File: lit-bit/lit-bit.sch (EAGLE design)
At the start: 10 parts, among them IC1 ATMEGA32U4-MU, SW1 SPST_TACT-KMR2, U1 S-1317A33-M5T1U4, X3 microUSB, Y1 8MHz

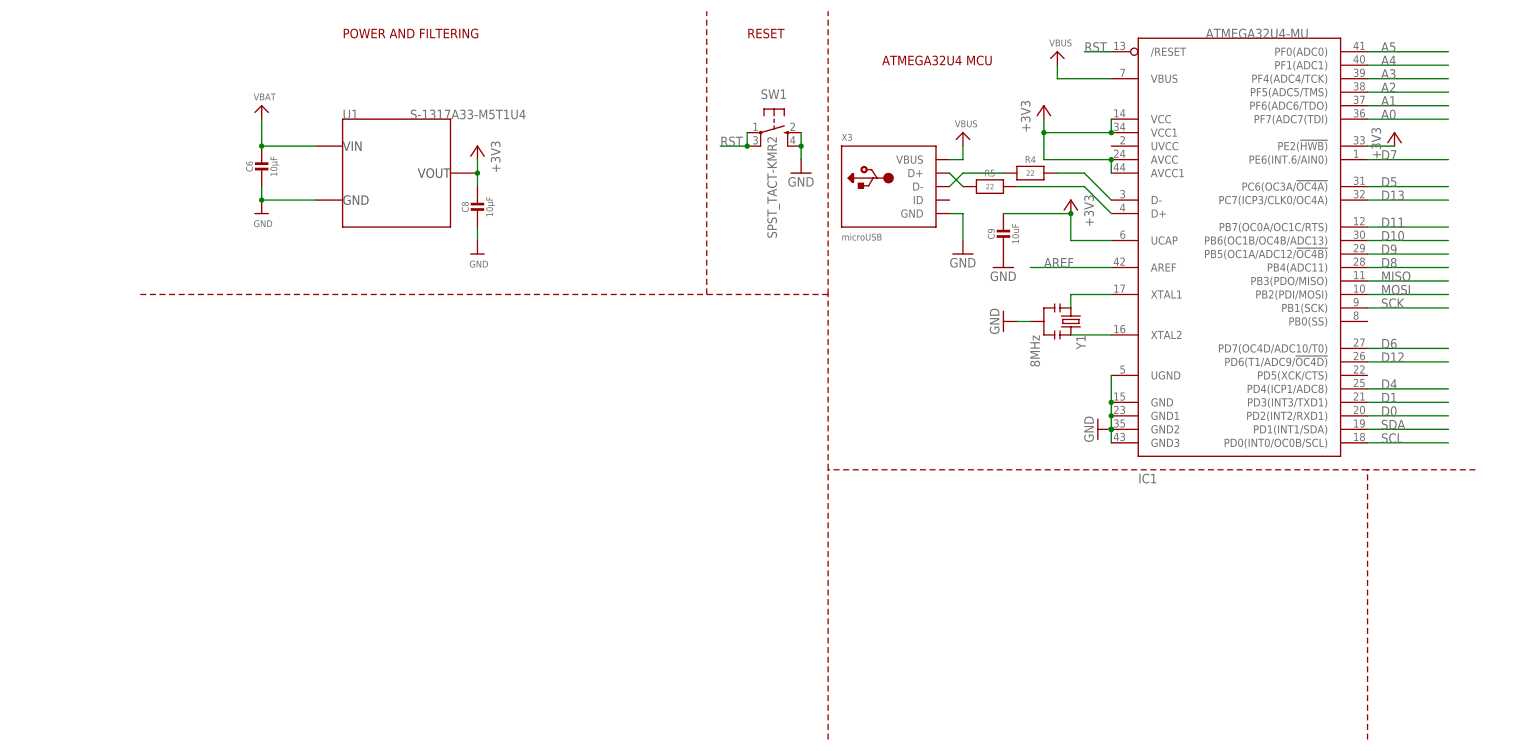
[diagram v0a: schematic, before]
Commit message: added power circuitry
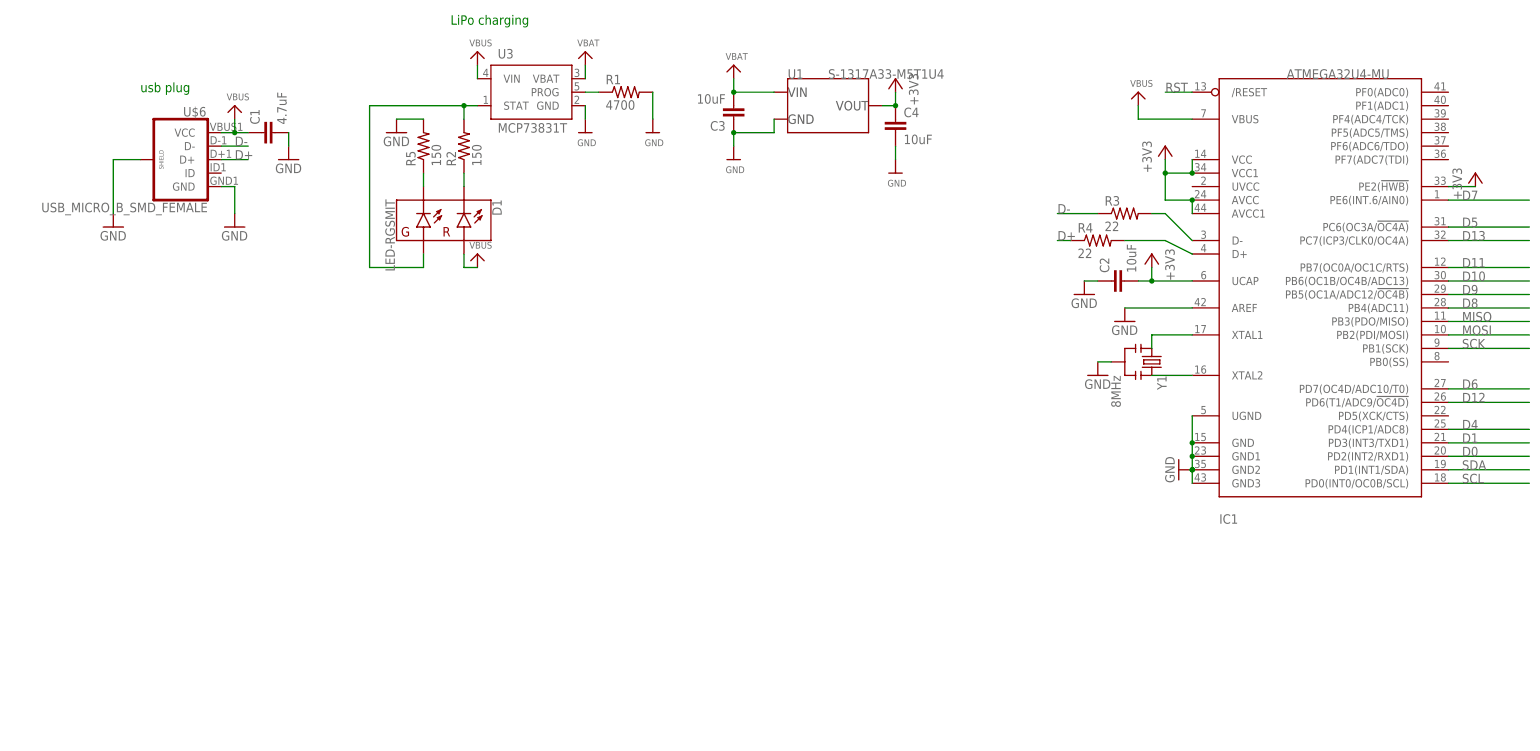
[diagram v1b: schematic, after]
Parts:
- removed C6, C8: 10µF, microbuilder:CAP_CERAMIC0805-NOOUTLINE
- removed C9: 10uF, microbuilder:CAP_CERAMIC0805-NOOUTLINE
- removed SW1: SPST_TACT-KMR2, adafruit:SPST_TACT-KMR2
- removed X3: microUSB, microbuilder:USB_MICRO_20329_V2
- added C1: 4.7uF, SCADA_CUSTOM_LIBRARY:CAP_NONPOL_0805
- added C2, C3, C4: 10uF, SCADA_CUSTOM_LIBRARY:CAP_NONPOL_0805
- added D1: LED-RGSMIT, SCADA_CUSTOM_LIBRARY:LED-RGSMIT
- added R1: 4700, SCADA_CUSTOM_LIBRARY:RES-0805
- added R2: 150, SCADA_CUSTOM_LIBRARY:RES-0805
- added R3: 22, SCADA_CUSTOM_LIBRARY:RES-0805
- added U$6: USB_MICRO_B_SMD_FEMALE, SCADA_CUSTOM_LIBRARY:USB_MICRO_B_SMD_FEMALE
- added U3: MCP73831T, SCADA_CUSTOM_LIBRARY:MCP73831T
- R4: device microbuilder:RESISTOR_0603_NOOUT -> SCADA_CUSTOM_LIBRARY:RES-0805
- R5: value 22 -> 150; device microbuilder:RESISTOR_0603_NOOUT -> SCADA_CUSTOM_LIBRARY:RES-0805
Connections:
- removed net A0: IC1.PF7(ADC7(TDI)
- removed net A1: IC1.PF6(ADC6/TDO)
- removed net A2: IC1.PF5(ADC5/TMS)
- removed net A3: IC1.PF4(ADC4/TCK)
- removed net A4: IC1.PF1(ADC1)
- removed net A5: IC1.PF0(ADC0)
- removed net AREF: IC1.AREF
- removed net N$15: R5.1, X3.D+
- removed net N$16: R4.1, X3.D-
- new net N$1: IC1.D-, R3.2
- new net N$2: R1.1, U3.PROG
- new net N$3: D1.GA, R2.2, U3.STAT
- new net N$4: D1.RC, R2.1
- new net N$5: D1.GC, R5.1
- net +3V3: now also C2.2, C4.1; no longer C8.1, C9.1
- net D+: now also R4.1, R4.2, U$6.D+; no longer R5.2
- net D-: now also R3.1, U$6.D-; no longer IC1.D-, R4.2
- net GND: now also C1.2, C2.1, C3.1, C4.2, IC1.AREF, R1.2, R5.2, U$6.GND, U$6.SHIELD, U3.GND; no longer C6.2, C8.2, C9.2, SW1.S, SW1.S1, X3.GND
- net RST: no longer SW1.P, SW1.P1
- net VBAT: now also C3.2, U3.VBAT; no longer C6.1
- net VBUS: now also C1.1, D1.RA, U$6.VCC, U3.VIN; no longer X3.VBUS
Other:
- note added: "LiPo charging"
- note added: "usb plug"
- note removed: "ATMEGA32U4 MCU"
- note removed: "POWER AND FILTERING"
- note removed: "RESET"
- moved on the sheet: IC1, U1, Y1

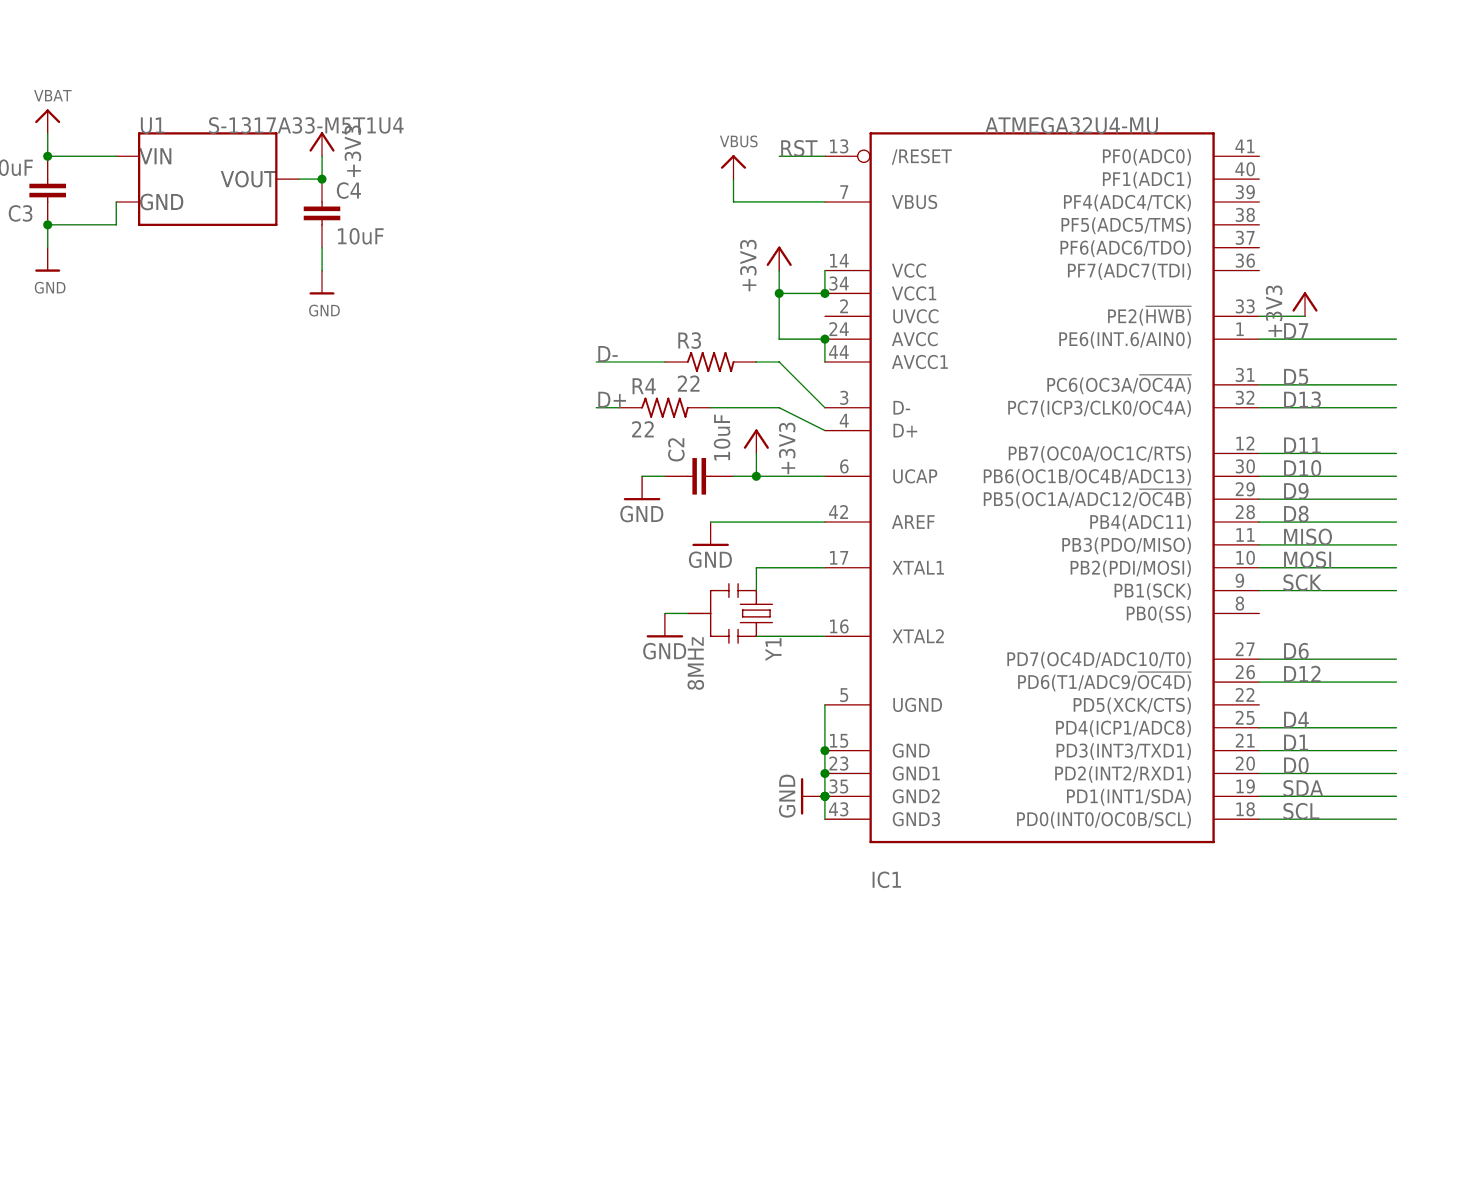
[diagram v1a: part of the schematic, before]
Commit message: imported TQFN package for 32u4
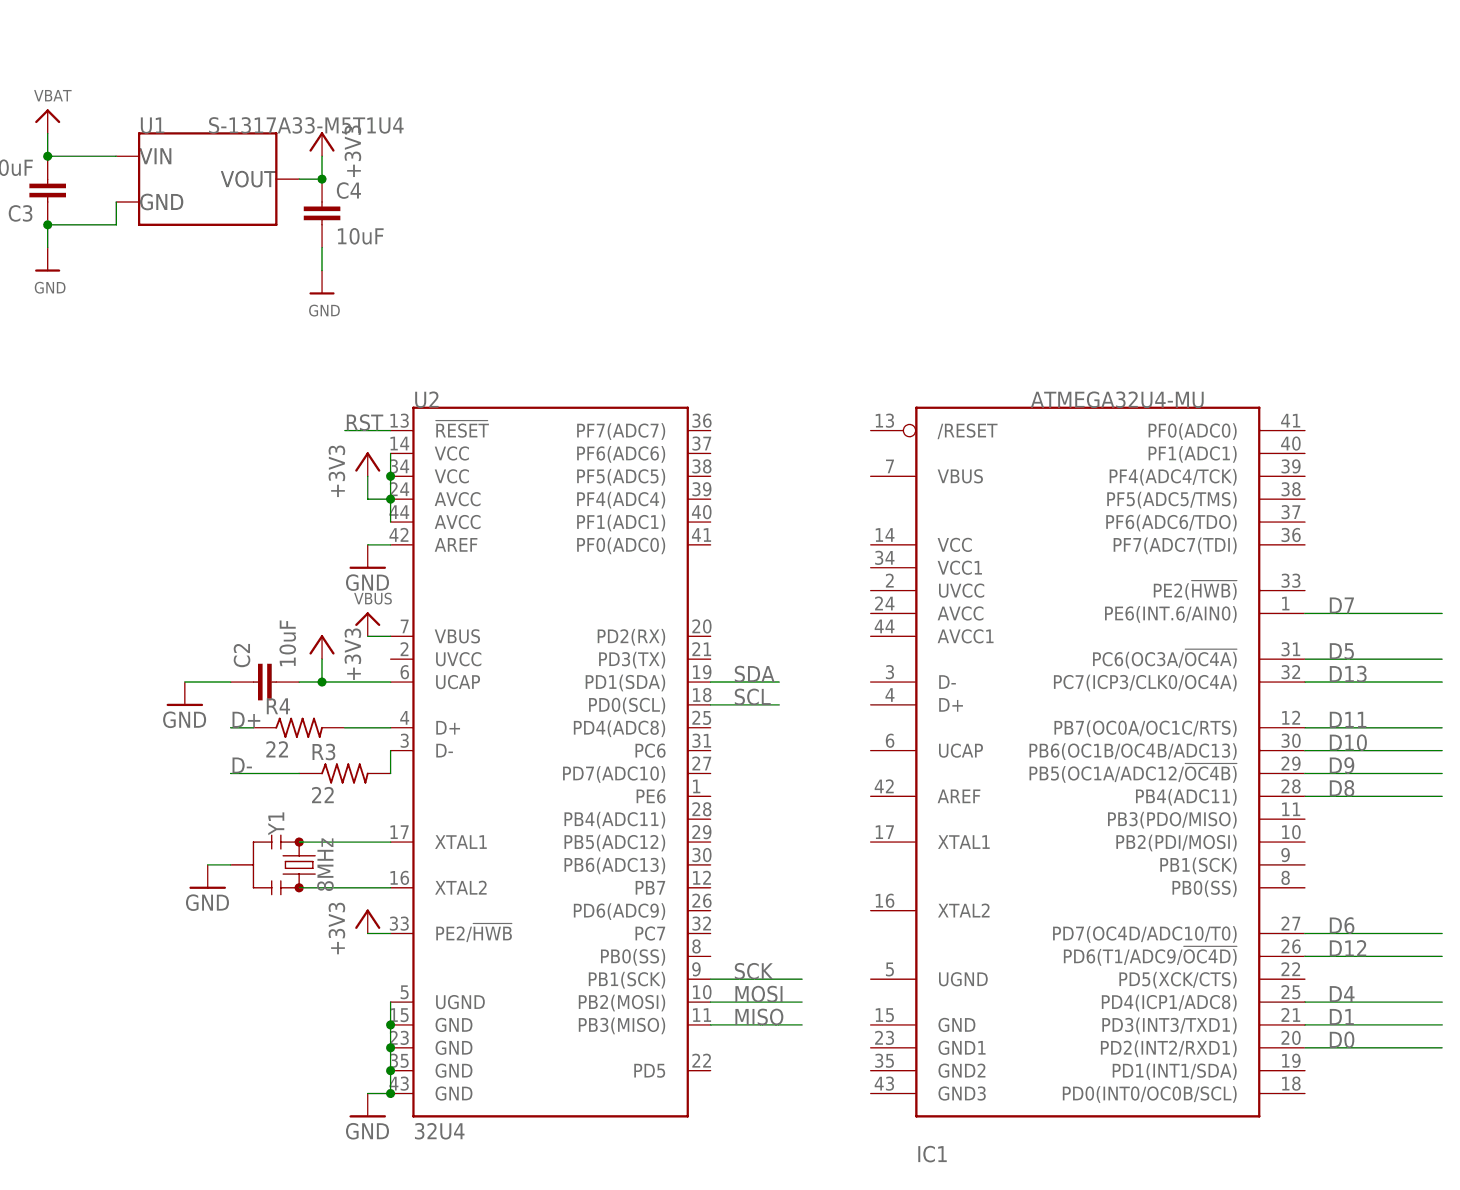
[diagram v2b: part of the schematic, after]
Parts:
- added U2: 32U4, SCADA_CUSTOM_LIBRARY:ATMEGA32U4TQFP-44
- Y1: device SparkFun:RESONATORSMD -> SCADA_CUSTOM_LIBRARY:RESONATOR-8MHZSMD_3.2X1.3
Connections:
- removed net N$11: IC1.XTAL2, Y1.3
- removed net N$12: IC1.XTAL1, Y1.1
- new net N$6: R3.2, U2.D-
- new net N$7: U2.XTAL2, Y1.3
- net +3V3: now also U2.AVCC@24, U2.AVCC@44, U2.PE2/!HWB, U2.UCAP, U2.VCC@14, U2.VCC@34; no longer IC1.AVCC, IC1.AVCC1, IC1.PE2(!HWB), IC1.UCAP, IC1.VCC, IC1.VCC1
- net D+: now also U2.D+; no longer IC1.D+
- net GND: now also U2.AREF, U2.GND@15, U2.GND@23, U2.GND@35, U2.GND@43, U2.UGND; no longer IC1.AREF, IC1.GND, IC1.GND1, IC1.GND2, IC1.GND3, IC1.UGND
- net MISO: now also U2.PB3(MISO); no longer IC1.PB3(PDO/MISO)
- net MOSI: now also U2.PB2(MOSI); no longer IC1.PB2(PDI/MOSI)
- net N$1: now also U2.XTAL1, Y1.1; no longer IC1.D-, R3.2
- net RST: now also U2.!RESET; no longer IC1./RESET
- net SCK: now also U2.PB1(SCK); no longer IC1.PB1(SCK)
- net SCL: now also U2.PD0(SCL); no longer IC1.PD0(INT0/OC0B/SCL)
- net SDA: now also U2.PD1(SDA); no longer IC1.PD1(INT1/SDA)
- net VBUS: now also U2.VBUS; no longer IC1.VBUS
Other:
- moved on the sheet: C2, IC1, R3, R4

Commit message: removed QFN 32u4
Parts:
- removed IC1: ATMEGA32U4-MU, microbuilder:ATMEGA32U4-MU
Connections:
- removed net D0: IC1.PD2(INT2/RXD1)
- removed net D1: IC1.PD3(INT3/TXD1)
- removed net D10: IC1.PB6(OC1B/OC4B/ADC13)
- removed net D11: IC1.PB7(OC0A/OC1C/RTS)
- removed net D12: IC1.PD6(T1/ADC9/!OC4D)
- removed net D13: IC1.PC7(ICP3/CLK0/OC4A)
- removed net D4: IC1.PD4(ICP1/ADC8)
- removed net D5: IC1.PC6(OC3A/!OC4A)
- removed net D6: IC1.PD7(OC4D/ADC10/T0)
- removed net D7: IC1.PE6(INT.6/AIN0)
- removed net D8: IC1.PB4(ADC11)
- removed net D9: IC1.PB5(OC1A/ADC12/!OC4B)
- new net N$10: U2.PB7
- new net N$11: U2.PB6(ADC13)
- new net N$12: U2.PB5(ADC12)
- new net N$13: U2.PB4(ADC11)
- new net N$14: U2.PD7(ADC10)
- new net N$15: U2.PD3(TX)
- new net N$16: U2.PD2(RX)
- new net N$17: U2.PD6(ADC9)
- new net N$18: U2.PC7
- new net N$19: U2.PD4(ADC8)
- new net N$8: U2.PE6
- new net N$9: U2.PC6
- net GND: now also U2.PF0(ADC0), U2.PF1(ADC1), U2.PF4(ADC4), U2.PF5(ADC5), U2.PF6(ADC6), U2.PF7(ADC7)
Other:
- moved on the sheet: C1, C2, C3, C4, D1, R1, R2, R3, R4, R5, U$6, U1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
